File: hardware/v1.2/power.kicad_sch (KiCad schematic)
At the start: 36 parts, among them U1 ECP5U_25F_CABGA256, U2 TLV62569DBV, U3 TLV62569DBV, U4 TLV62569DBV

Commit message: Trying to document my journey :)
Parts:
- renumbered C9 to C10, C10 to C11, C11 to C12, C12 to C13, C13 to C14, C14 to C15, C15 to C16, C16 to C17, C17 to C18, C18 to C19, C19 to C20, C20 to C21, C21 to C22, C22 to C23, C23 to C24, C24 to C25, C3 to C4, C4 to C5, C5 to C6, C6 to C7, C7 to C8, C8 to C9

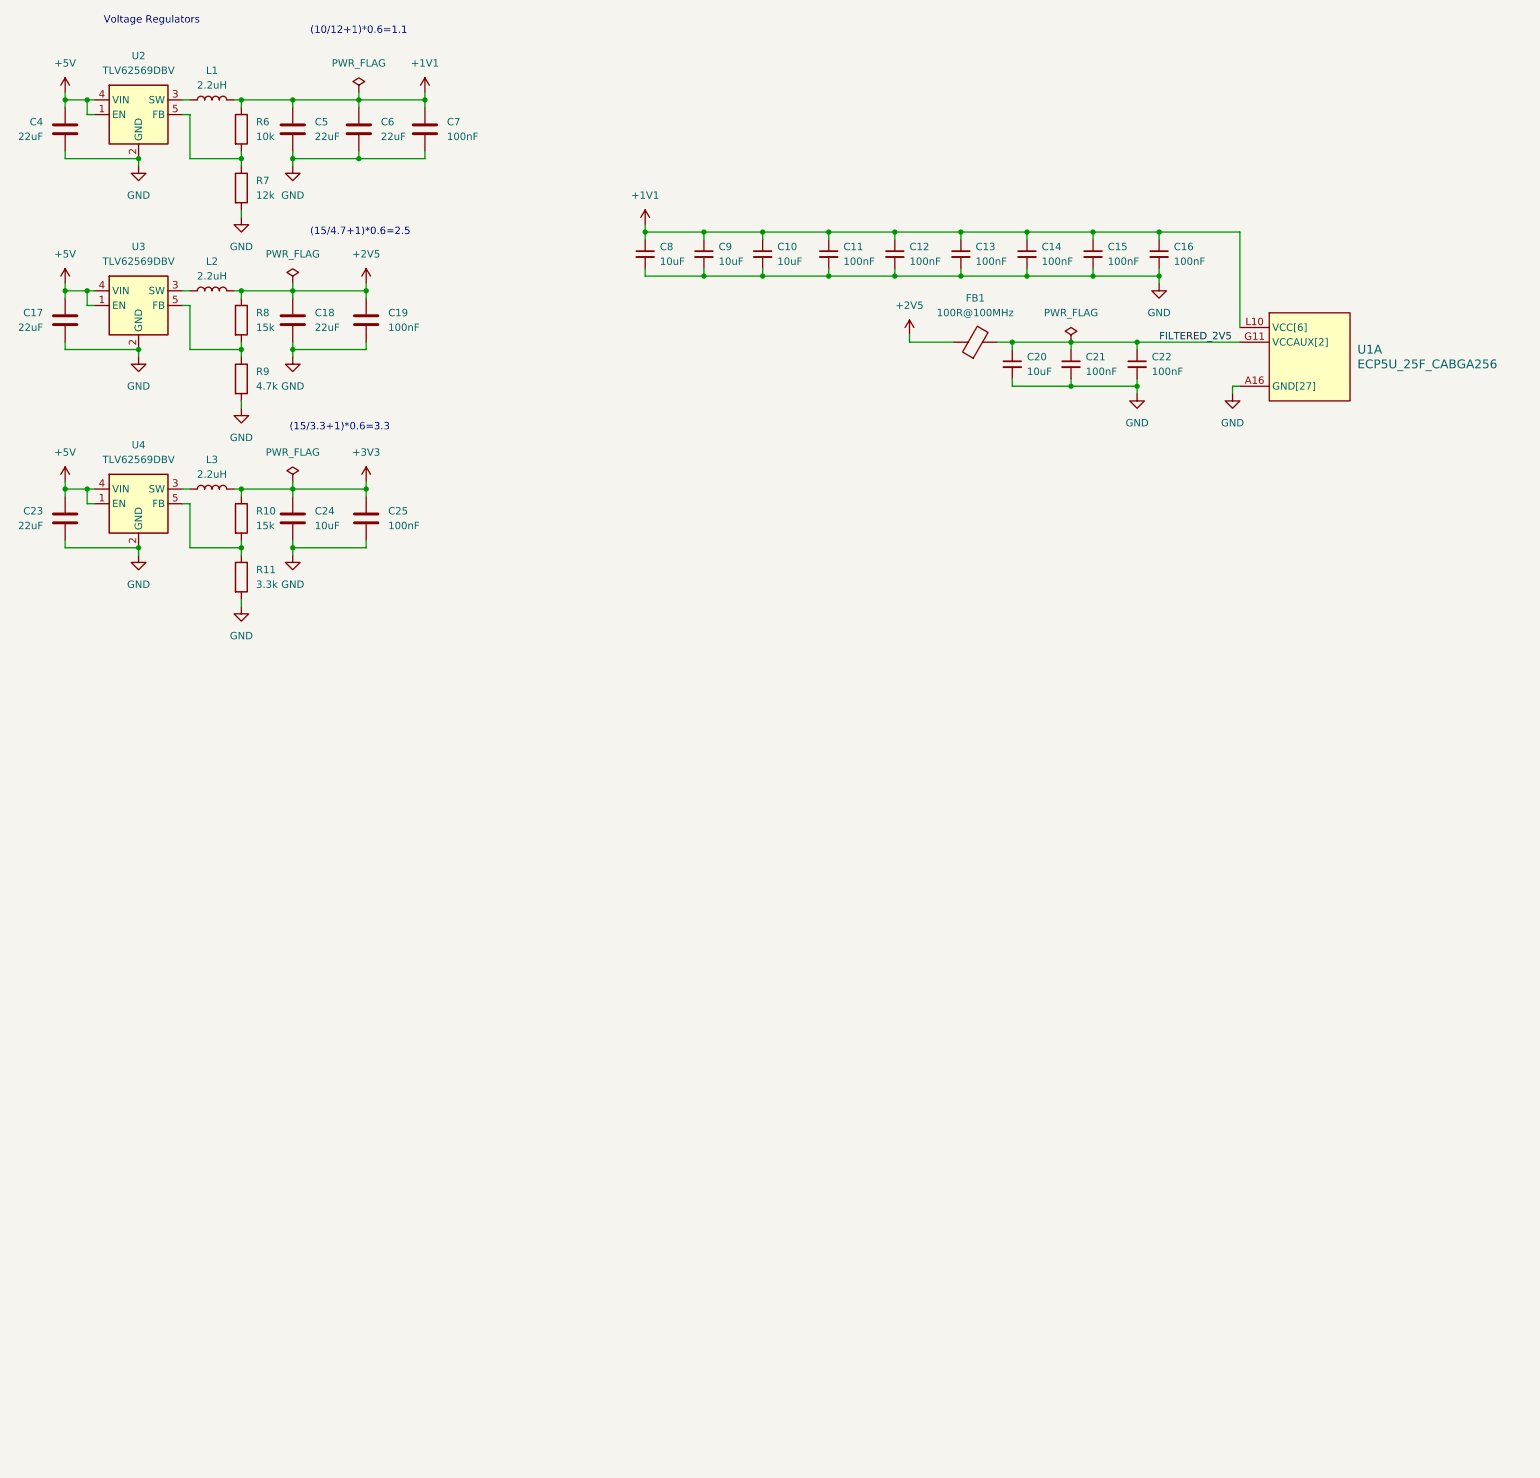
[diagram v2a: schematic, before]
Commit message: Custom ECP5-CABGA256 symbol
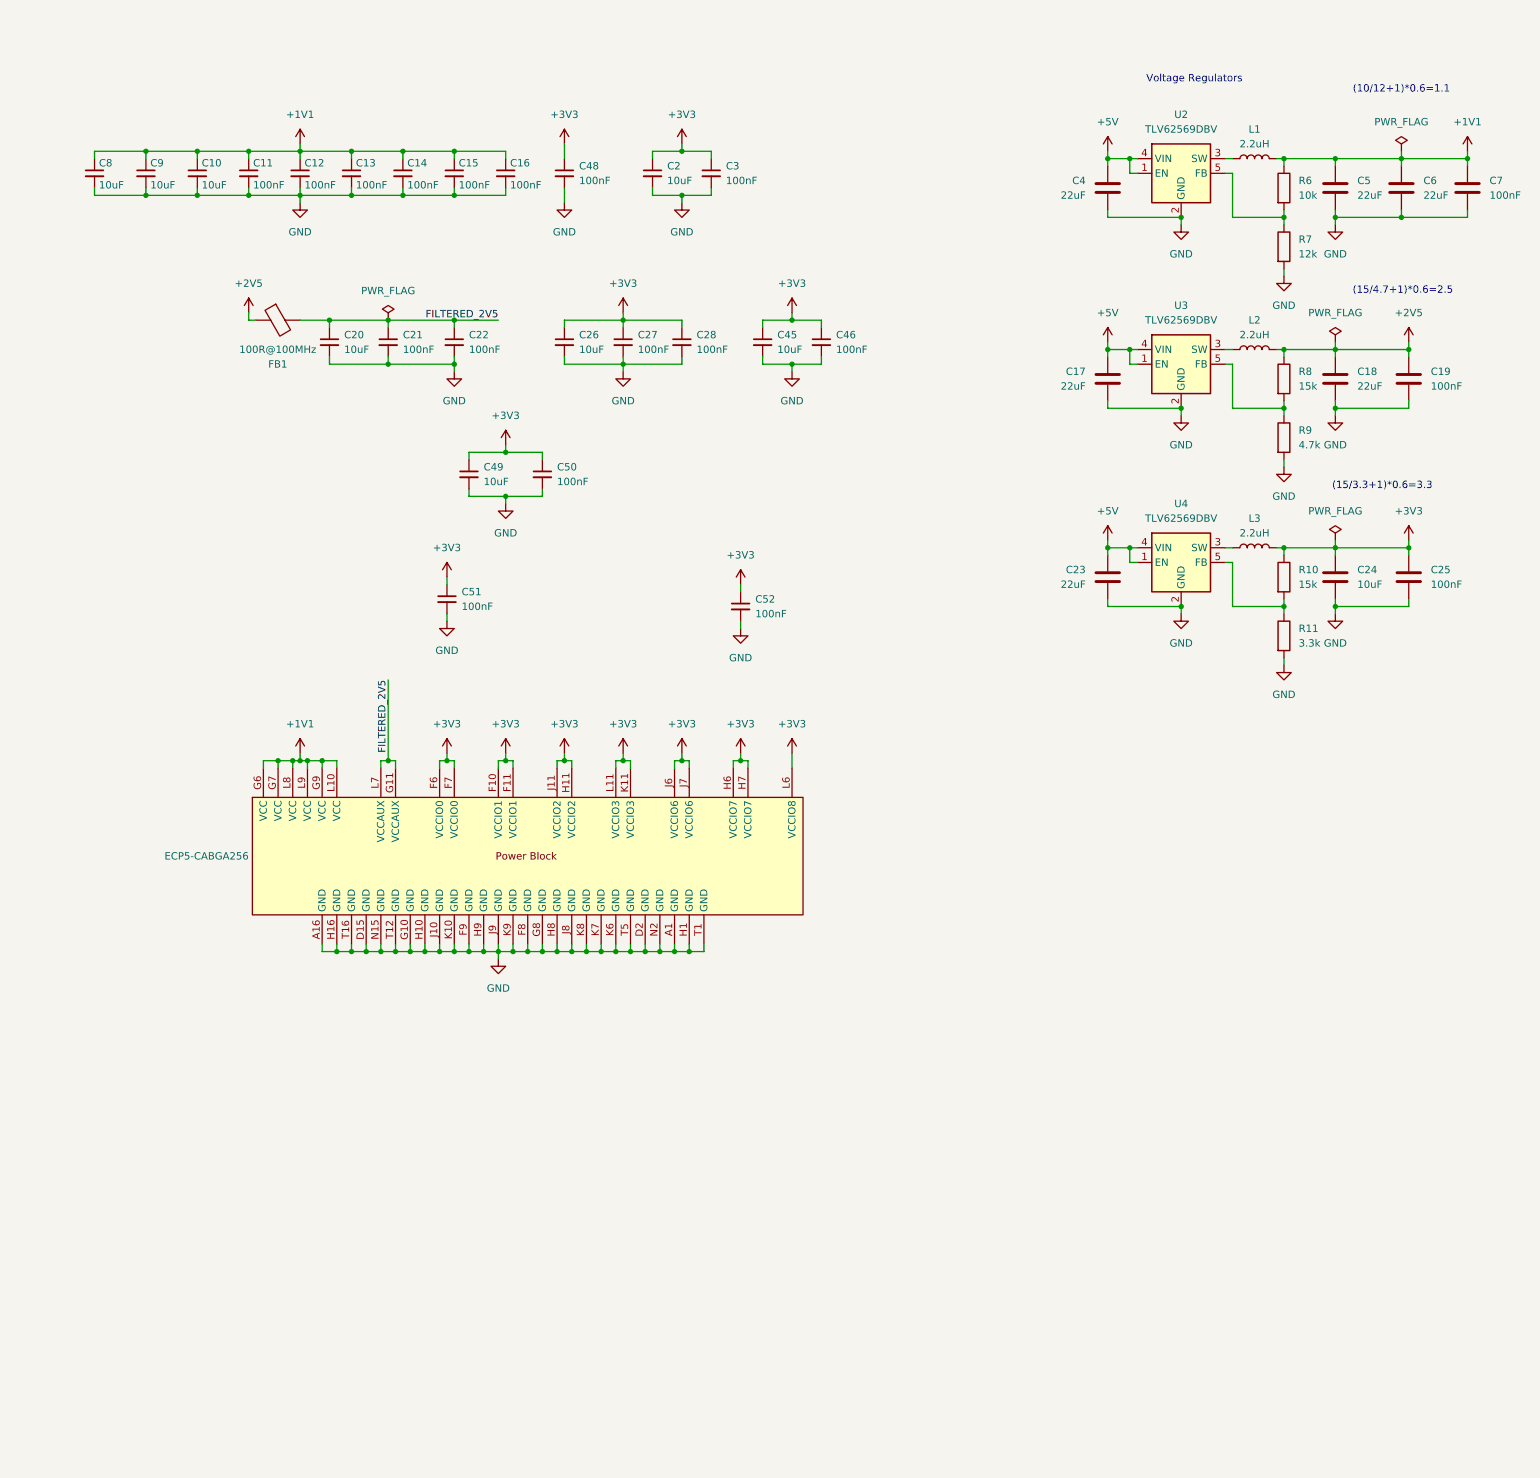
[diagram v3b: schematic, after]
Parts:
- removed U1: ECP5U_25F_CABGA256, Package_BGA:BGA-256_14.0x14.0mm_Layout16x16_P0.8mm_Ball0.45mm_Pad0.32mm_NSMD, symbol josh:ECP5U_12_CABGA256
- added C2, C26, C45, C49: 10uF, Capacitor_SMD:C_0603_1608Metric, symbol Device:C_Small
- added C27, C28, C3, C46, C48, C50, C51, C52: 100nF, Capacitor_SMD:C_0402_1005Metric, symbol Device:C_Small
- added U1: ECP5-CABGA256, Package_BGA:BGA-256_14.0x14.0mm_Layout16x16_P0.8mm_Ball0.45mm_Pad0.32mm_NSMD, symbol icepi-lib:LFE5U-25F-6BG256x
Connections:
- net +1V1: now also U1.G6 (VCC), U1.G7 (VCC), U1.G9 (VCC), U1.L10 (VCC), U1.L8 (VCC), U1.L9 (VCC)
- net +3V3: now also C2.1, C26.1, C27.1, C28.1, C3.1, C45.1, C46.1, C48.1, C49.1, C50.1, C51.1, C52.1, U1.F10 (VCCIO1), U1.F11 (VCCIO1), U1.F6 (VCCIO0), U1.F7 (VCCIO0), U1.H11 (VCCIO2), U1.H6 (VCCIO7), U1.H7 (VCCIO7), U1.J11 (VCCIO2), U1.J6 (VCCIO6), U1.J7 (VCCIO6), U1.K11 (VCCIO3), U1.L11 (VCCIO3), U1.L6 (VCCIO8)
- net FILTERED_2V5: now also U1.G11 (VCCAUX), U1.L7 (VCCAUX)
- net GND: now also C2.2, C26.2, C27.2, C28.2, C3.2, C45.2, C46.2, C48.2, C49.2, C50.2, C51.2, C52.2, U1.A1 (GND), U1.A16 (GND), U1.D15 (GND), U1.D2 (GND), U1.F8 (GND), U1.F9 (GND), U1.G10 (GND), U1.G8 (GND), U1.H1 (GND), U1.H10 (GND), U1.H16 (GND), U1.H8 (GND), U1.H9 (GND), U1.J10 (GND), U1.J8 (GND), U1.J9 (GND), U1.K10 (GND), U1.K6 (GND), U1.K7 (GND), U1.K8 (GND), U1.K9 (GND), U1.N15 (GND), U1.N2 (GND), U1.T1 (GND), U1.T12 (GND), U1.T16 (GND), U1.T5 (GND)
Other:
- moved on the sheet: C10, C11, C12, C13, C14, C15, C16, C17, C18, C19, C20, C21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

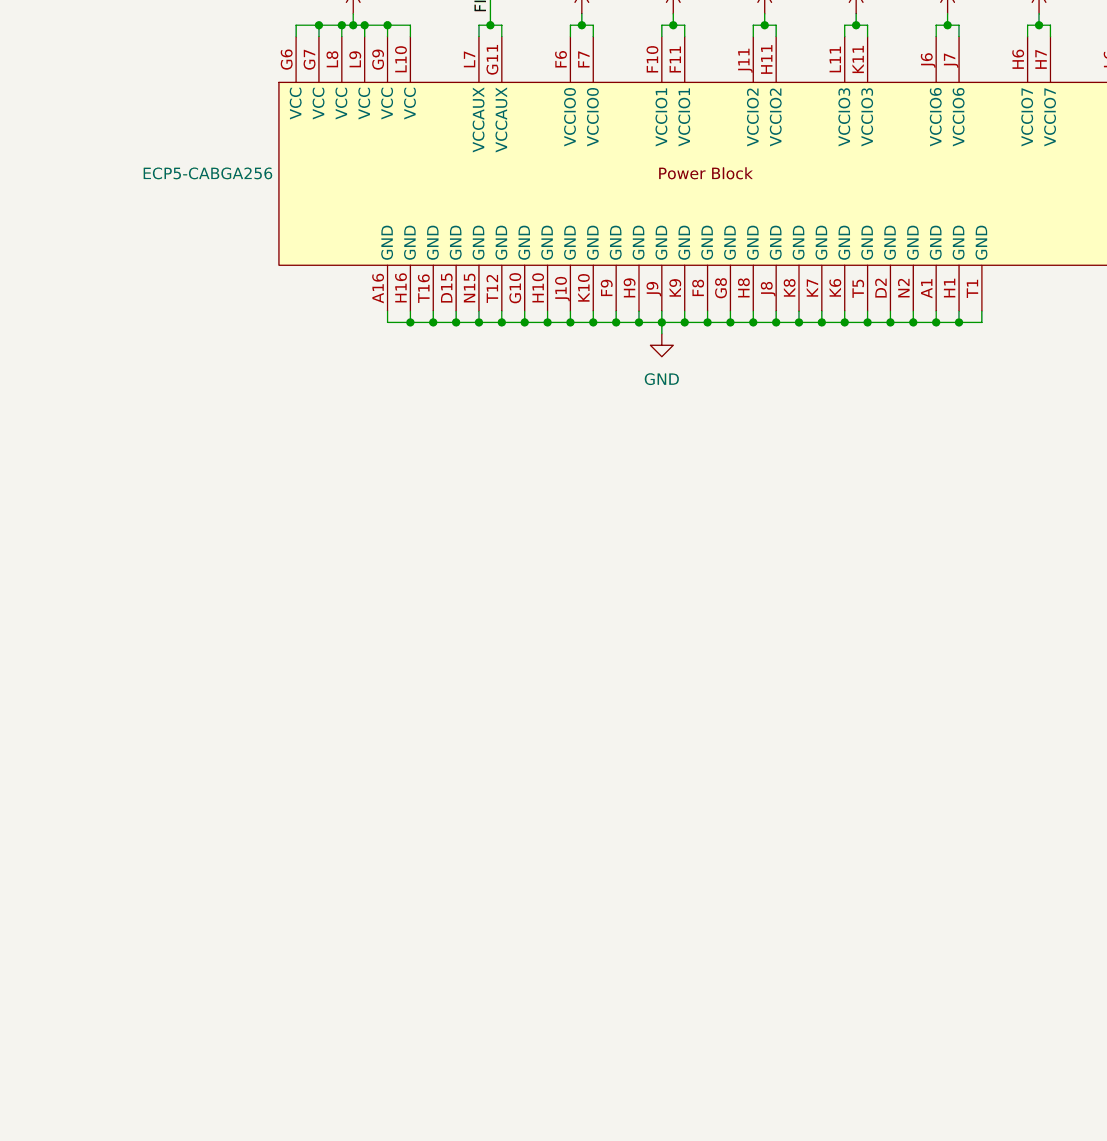
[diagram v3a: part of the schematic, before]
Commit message: UART to PS2 converter
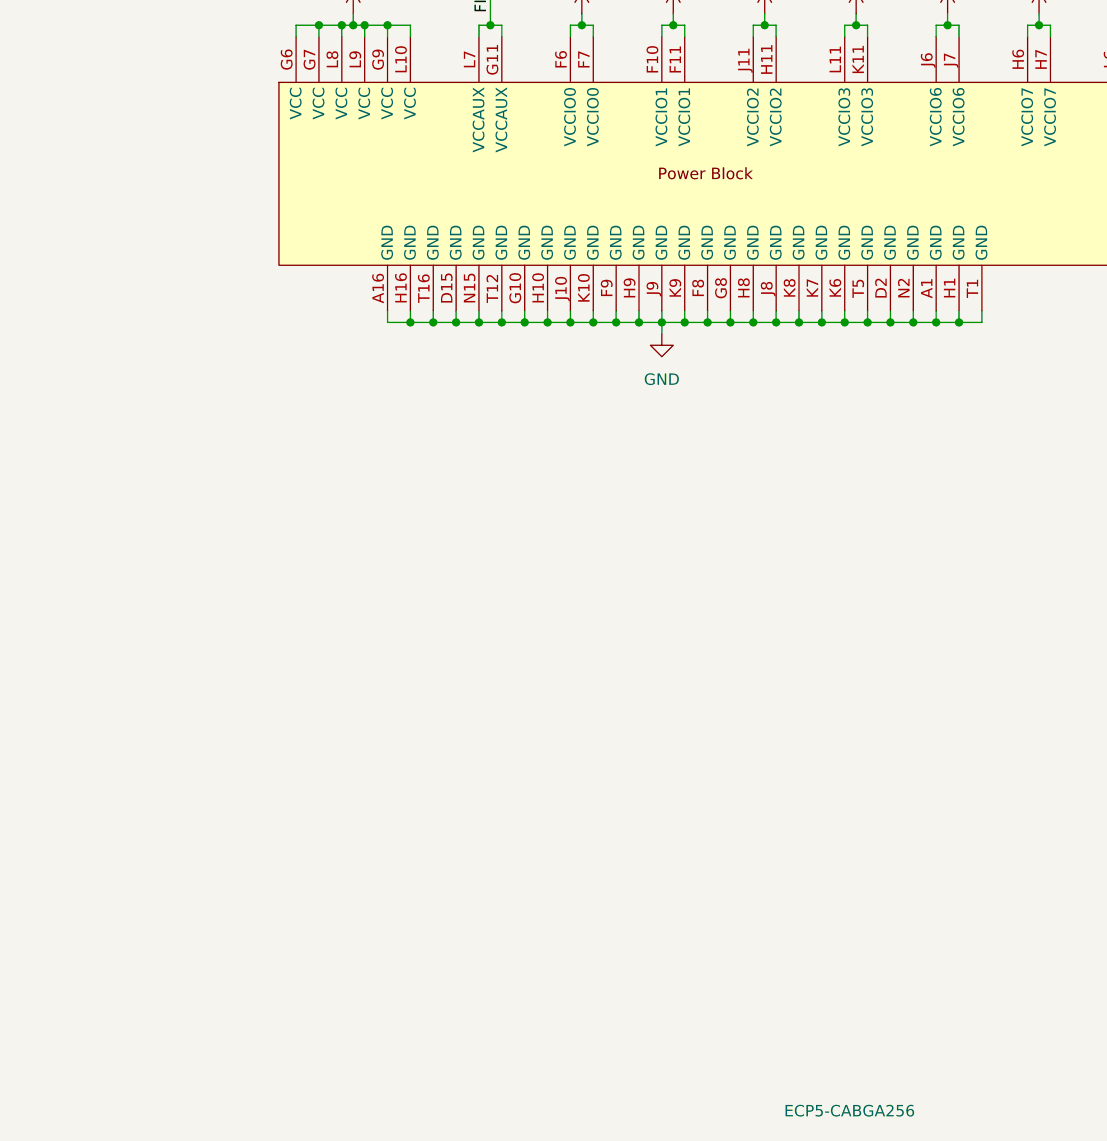
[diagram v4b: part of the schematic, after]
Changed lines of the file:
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@@
 		)
 		(property "Value" "ECP5-CABGA256"
-			(at 55.88 160.02 0)
+			(at 112.6333 264.16 0)
 			(effects
 				(font
 					(size 1.27 1.27)
 				)
-				(justify right)
+				(justify left)
 			)
 		)
@@
 		)
 		(instances
-			(project "icepi-zero"
+			(project ""
+				(path "/f88da08e-cf42-4d03-a08f-3f602fe6658d/17c9c9b3-f379-4e1f-a876-d3fcf0529a4d"
+					(reference "U1")
+					(unit 1)
+				)
 				(path "/f88da08e-cf42-4d03-a08f-3f602fe6658d/a9c02a11-f344-487c-ac67-1be6ae5dcf49"
 					(reference "U1")
